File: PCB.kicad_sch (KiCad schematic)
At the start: 48 parts, among them K1 G5LE-1A_DC3, K2 G5LE-1A_DC3, K3 G5LE-1, K4 G5LE-1, K6 G5LE-1, K7 G5LE-1A_DC3, Q1 DMN65D8L-7, Q2 DMN65D8L-7, Q3 DMN65D8L-7, Q4 DMN65D8L-7, Q5 DMN65D8L-7, Q6 DMN65D8L-7, SW1 Local DI0 (onoff), SW3 Local DI2 (decspeed), SW5 Local DI1 (incspeed), U1 WeMos_D1_mini

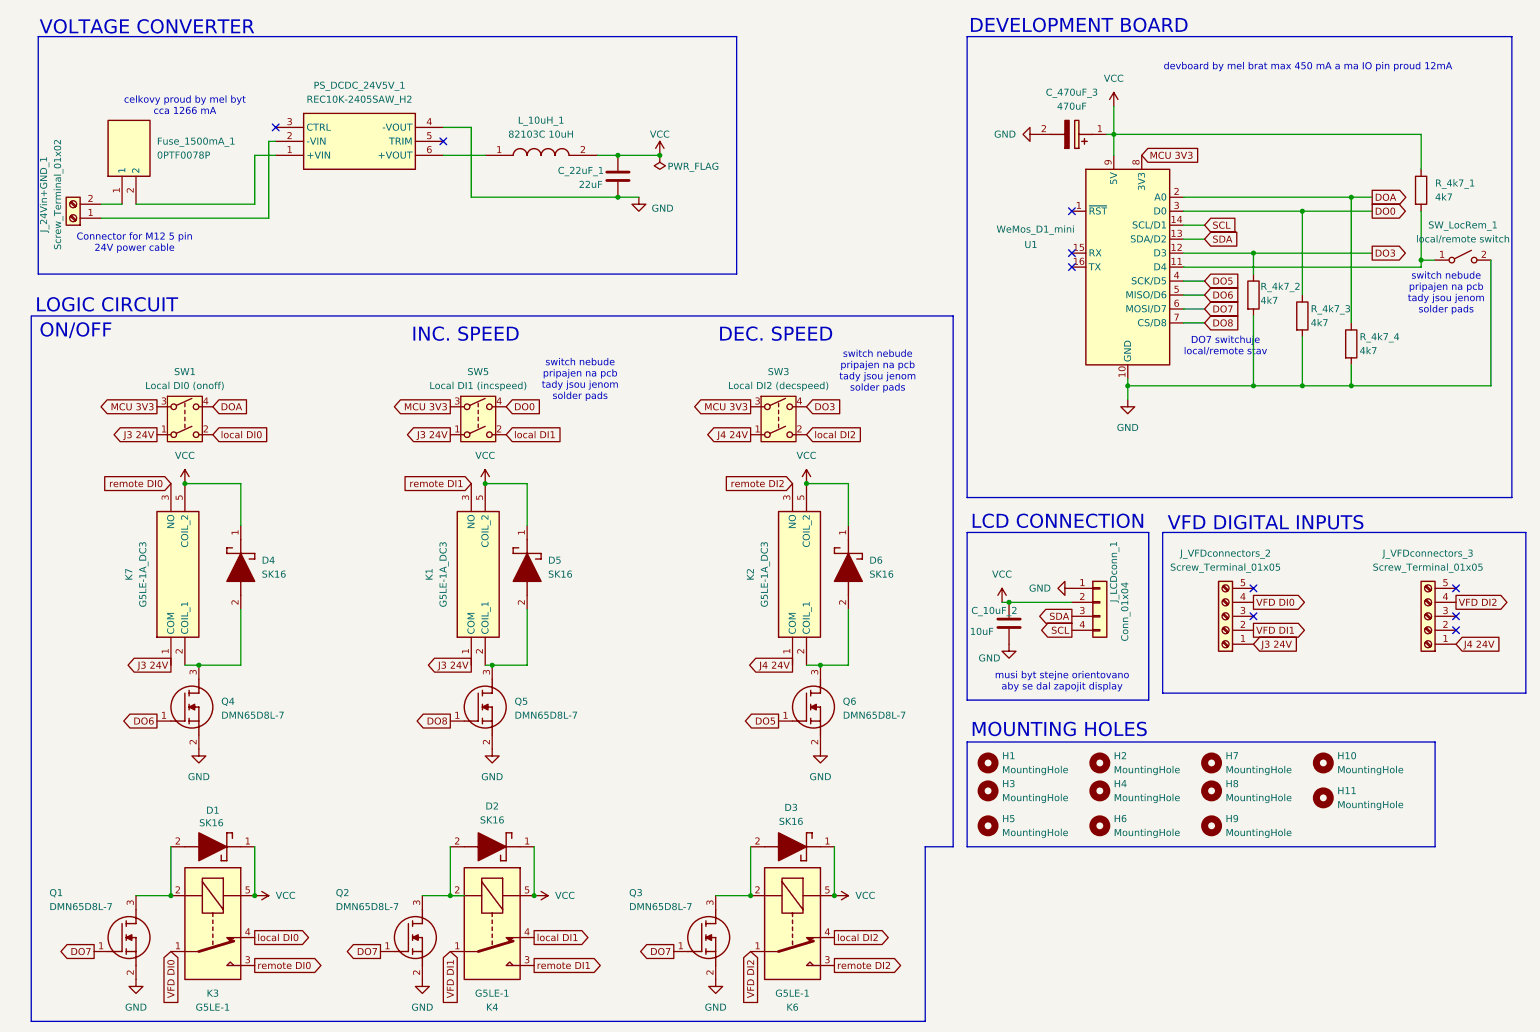
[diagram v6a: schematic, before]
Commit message: zmena nazvu v schemu logickym obvodu
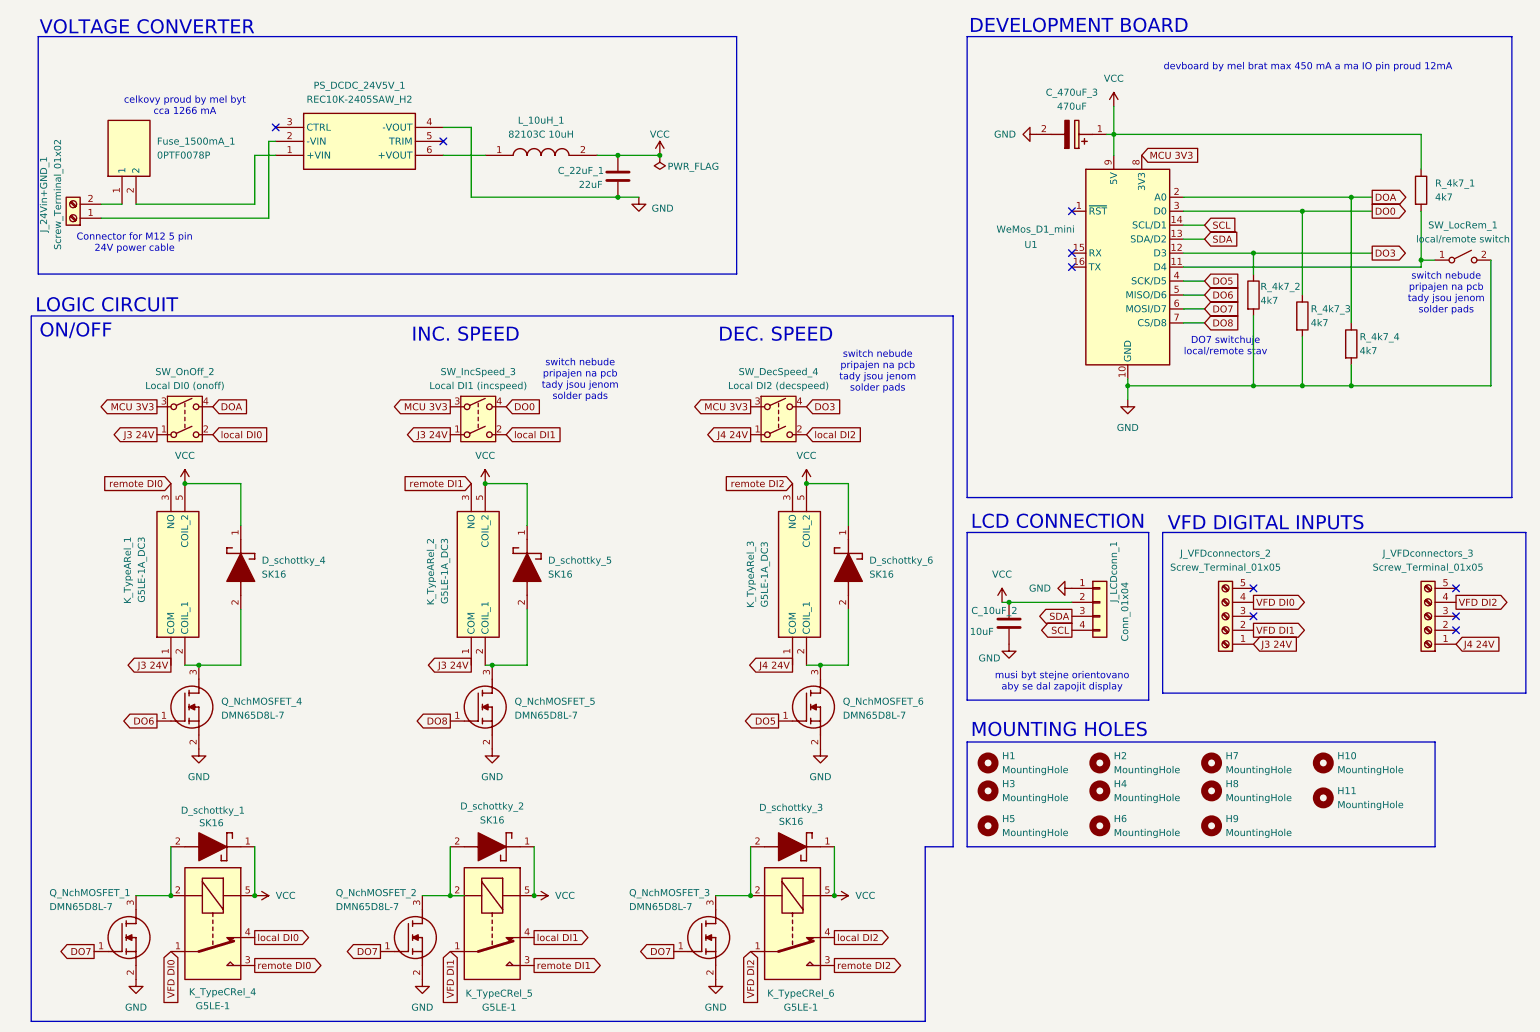
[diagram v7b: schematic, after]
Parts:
- renumbered D1 to D_schottky_1, D2 to D_schottky_2, D3 to D_schottky_3, D4 to D_schottky_4, D5 to D_schottky_5, D6 to D_schottky_6, K7 to K_TypeARel_1, K1 to K_TypeARel_2, K2 to K_TypeARel_3, K3 to K_TypeCRel_4, K4 to K_TypeCRel_5, K6 to K_TypeCRel_6, Q1 to Q_NchMOSFET_1, Q2 to Q_NchMOSFET_2, Q3 to Q_NchMOSFET_3, Q4 to Q_NchMOSFET_4, Q5 to Q_NchMOSFET_5, Q6 to Q_NchMOSFET_6, SW3 to SW_DecSpeed_4, SW5 to SW_IncSpeed_3, SW1 to SW_OnOff_2
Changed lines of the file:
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@@
 		(on_board yes)
 		(dnp no)
-		(property "Reference" "Q2"
+		(property "Reference" "Q_NchMOSFET_2"
 			(at 68.072 173.482 0)
 			(effects
@@
 			(project "PCB"
 				(path "/a03e0b08-fd2d-4304-b838-c1c22de42e47"
-					(reference "Q2")
+					(reference "Q_NchMOSFET_2")
 					(unit 1)
 				)
@@
 		(dnp no)
 		(fields_autoplaced yes)
-		(property "Reference" "D4"
+		(property "Reference" "D_schottky_4"
 			(at 54.61 113.0299 90)
 			(effects
@@
 			(project "PCB"
 				(path "/a03e0b08-fd2d-4304-b838-c1c22de42e47"
-					(reference "D4")
+					(reference "D_schottky_4")
 					(unit 1)
 				)
@@
 		(dnp no)
 		(fields_autoplaced yes)
-		(property "Reference" "D6"
+		(property "Reference" "D_schottky_6"
 			(at 165.1 113.0299 90)
 			(effects
@@
 			(project "PCB"
 				(path "/a03e0b08-fd2d-4304-b838-c1c22de42e47"
-					(reference "D6")
+					(reference "D_schottky_6")
 					(unit 1)
 				)
@@
 		(dnp no)
 		(fields_autoplaced yes)
-		(property "Reference" "SW5"
+		(property "Reference" "SW_IncSpeed_3"
 			(at 93.98 78.74 0)
 			(effects
@@
 			(project ""
 				(path "/a03e0b08-fd2d-4304-b838-c1c22de42e47"
-					(reference "SW5")
+					(reference "SW_IncSpeed_3")
 					(unit 1)
 				)
@@
 		(on_board yes)
 		(dnp no)
-		(property "Reference" "Q4"
+		(property "Reference" "Q_NchMOSFET_4"
 			(at 47.244 138.684 0)
 			(effects
@@
 			(project "PCB"
 				(path "/a03e0b08-fd2d-4304-b838-c1c22de42e47"
-					(reference "Q4")
+					(reference "Q_NchMOSFET_4")
 					(unit 1)
 				)
@@
 		(dnp no)
 		(fields_autoplaced yes)
-		(property "Reference" "SW1"
+		(property "Reference" "SW_OnOff_2"
 			(at 40.64 78.74 0)
 			(effects
@@
 			(project "PCB"
 				(path "/a03e0b08-fd2d-4304-b838-c1c22de42e47"
-					(reference "SW1")
+					(reference "SW_OnOff_2")
 					(unit 1)
 				)
@@
 		(on_board yes)
 		(dnp no)
-		(fields_autoplaced yes)
-		(property "Reference" "K6"
-			(at 151.13 194.31 90)
+		(property "Reference" "K_TypeCRel_6"
+			(at 152.654 191.77 90)
 			(effects
 				(font
@@
 		)
 		(property "Value" "G5LE-1"
-			(at 151.13 191.77 90)
+			(at 152.654 194.31 90)
 			(effects
 				(font
@@
 			(project "PCB"
 				(path "/a03e0b08-fd2d-4304-b838-c1c22de42e47"
-					(reference "K6")
+					(reference "K_TypeCRel_6")
 					(unit 1)
 				)
@@
 		(on_board yes)
 		(dnp no)
-		(property "Reference" "K3"
-			(at 45.72 191.77 90)
+		(property "Reference" "K_TypeCRel_4"
+			(at 47.498 191.516 90)
 			(effects
 				(font
@@
 		)
 		(property "Value" "G5LE-1"
-			(at 45.72 194.31 90)
+			(at 45.72 194.056 90)
 			(effects
 				(font
@@
 			(project ""
 				(path "/a03e0b08-fd2d-4304-b838-c1c22de42e47"
-					(reference "K3")
+					(reference "K_TypeCRel_4")
 					(unit 1)
 				)
@@
 		(on_board yes)
 		(dnp no)
-		(property "Reference" "D1"
+		(property "Reference" "D_schottky_1"
 			(at 45.72 158.496 0)
 			(effects
@@
 			(project ""
 				(path "/a03e0b08-fd2d-4304-b838-c1c22de42e47"
-					(reference "D1")
+					(reference "D_schottky_1")
 					(unit 1)
 				)
@@
 		(on_board yes)
 		(dnp no)
-		(property "Reference" "Q3"
+		(property "Reference" "Q_NchMOSFET_3"
 			(at 121.412 173.482 0)
 			(effects
@@
 			(project "PCB"
 				(path "/a03e0b08-fd2d-4304-b838-c1c22de42e47"
-					(reference "Q3")
+					(reference "Q_NchMOSFET_3")
 					(unit 1)
 				)
@@
 		(on_board yes)
 		(dnp no)
-		(property "Reference" "Q1"
+		(property "Reference" "Q_NchMOSFET_1"
 			(at 16.002 173.482 0)
 			(effects
@@
 			(project ""
 				(path "/a03e0b08-fd2d-4304-b838-c1c22de42e47"
-					(reference "Q1")
+					(reference "Q_NchMOSFET_1")
 					(unit 1)
 				)
@@
 		(on_board yes)
 		(dnp no)
-		(property "Reference" "Q5"
+		(property "Reference" "Q_NchMOSFET_5"
 			(at 100.584 138.684 0)
 			(effects
@@
 			(project "PCB"
 				(path "/a03e0b08-fd2d-4304-b838-c1c22de42e47"
-					(reference "Q5")
+					(reference "Q_NchMOSFET_5")
 					(unit 1)
 				)
@@
 		(on_board yes)
 		(dnp no)
-		(fields_autoplaced yes)
-		(property "Reference" "K2"
+		(property "Reference" "K_TypeARel_3"
 			(at 143.51 115.57 0)
 			(effects
@@
 			(project "PCB"
 				(path "/a03e0b08-fd2d-4304-b838-c1c22de42e47"
-					(reference "K2")
+					(reference "K_TypeARel_3")
 					(unit 1)
 				)
@@
 		(on_board yes)
 		(dnp no)
-		(property "Reference" "D3"
+		(property "Reference" "D_schottky_3"
 			(at 150.876 157.988 0)
 			(effects
@@
 			(project "PCB"
 				(path "/a03e0b08-fd2d-4304-b838-c1c22de42e47"
-					(reference "D3")
+					(reference "D_schottky_3")
 					(unit 1)
 				)
@@
 		(dnp no)
 		(fields_autoplaced yes)
-		(property "Reference" "SW3"
+		(property "Reference" "SW_DecSpeed_4"
 			(at 148.59 78.74 0)
 			(effects
@@
 			(project "PCB"
 				(path "/a03e0b08-fd2d-4304-b838-c1c22de42e47"
-					(reference "SW3")
+					(reference "SW_DecSpeed_4")
 					(unit 1)
 				)
@@
 		(on_board yes)
 		(dnp no)
-		(property "Reference" "D2"
+		(property "Reference" "D_schottky_2"
 			(at 96.52 157.734 0)
 			(effects
@@
 			(project "PCB"
 				(path "/a03e0b08-fd2d-4304-b838-c1c22de42e47"
-					(reference "D2")
+					(reference "D_schottky_2")
 					(unit 1)
 				)
@@
 		(on_board yes)
 		(dnp no)
-		(property "Reference" "Q6"
+		(property "Reference" "Q_NchMOSFET_6"
 			(at 160.274 138.684 0)
 			(effects
@@
 			(project "PCB"
 				(path "/a03e0b08-fd2d-4304-b838-c1c22de42e47"
-					(reference "Q6")
+					(reference "Q_NchMOSFET_6")
 					(unit 1)
 				)
@@
 		(on_board yes)
 		(dnp no)
-		(fields_autoplaced yes)
-		(property "Reference" "K7"
-			(at 30.48 115.57 0)
+		(property "Reference" "K_TypeARel_1"
+			(at 30.226 108.712 0)
 			(effects
 				(font
 					(size 1.27 1.27)
 				)
+				(justify right)
 			)
 		)
 		(property "Value" "G5LE-1A_DC3"
-			(at 33.02 115.57 0)
+			(at 32.766 108.712 0)
 			(effects
 				(font
 					(size 1.27 1.27)
 				)
+				(justify right)
 			)
 		)
@@
 			(project ""
 				(path "/a03e0b08-fd2d-4304-b838-c1c22de42e47"
-					(reference "K7")
+					(reference "K_TypeARel_1")
 					(unit 1)
 				)
@@
 		(on_board yes)
 		(dnp no)
-		(fields_autoplaced yes)
-		(property "Reference" "K4"
-			(at 96.52 194.31 90)
+		(property "Reference" "K_TypeCRel_5"
+			(at 97.79 191.77 90)
 			(effects
 				(font
@@
 		)
 		(property "Value" "G5LE-1"
-			(at 96.52 191.77 90)
+			(at 97.79 194.31 90)
 			(effects
 				(font
@@
 			(project "PCB"
 				(path "/a03e0b08-fd2d-4304-b838-c1c22de42e47"
-					(reference "K4")
+					(reference "K_TypeCRel_5")
 					(unit 1)
 				)
@@
 		(on_board yes)
 		(dnp no)
-		(fields_autoplaced yes)
-		(property "Reference" "K1"
-			(at 85.09 115.57 0)
+		(property "Reference" "K_TypeARel_2"
+			(at 85.344 108.966 0)
 			(effects
 				(font
 					(size 1.27 1.27)
 				)
+				(justify right)
 			)
 		)
 		(property "Value" "G5LE-1A_DC3"
-			(at 87.63 115.57 0)
+			(at 87.884 108.966 0)
 			(effects
 				(font
 					(size 1.27 1.27)
 				)
+				(justify right)
 			)
 		)
@@
 			(project "PCB"
 				(path "/a03e0b08-fd2d-4304-b838-c1c22de42e47"
-					(reference "K1")
+					(reference "K_TypeARel_2")
 					(unit 1)
 				)
@@
 		(dnp no)
 		(fields_autoplaced yes)
-		(property "Reference" "D5"
+		(property "Reference" "D_schottky_5"
 			(at 106.68 113.0299 90)
 			(effects
@@
 			(project "PCB"
 				(path "/a03e0b08-fd2d-4304-b838-c1c22de42e47"
-					(reference "D5")
+					(reference "D_schottky_5")
 					(unit 1)
 				)

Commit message: uprava textu na pcb aby byl videt i pod komponenty
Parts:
- H10, H11, H2: footprint MountingHole:MountingHole_5mm -> MountingHole:MountingHole_3mm
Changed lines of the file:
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@@
 			)
 		)
-		(property "Footprint" "MountingHole:MountingHole_5mm"
+		(property "Footprint" "MountingHole:MountingHole_3mm"
 			(at 247.65 149.86 0)
 			(effects
@@
 			)
 		)
-		(property "Footprint" "MountingHole:MountingHole_5mm"
+		(property "Footprint" "MountingHole:MountingHole_3mm"
 			(at 247.65 156.21 0)
 			(effects
@@
 			)
 		)
-		(property "Footprint" "MountingHole:MountingHole_5mm"
+		(property "Footprint" "MountingHole:MountingHole_3mm"
 			(at 207.01 149.86 0)
 			(effects
